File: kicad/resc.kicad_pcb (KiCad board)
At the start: 4 copper layers, 70 x 85 mm, 166 parts, among them J1 CAN, J10 LED2, J2 HALL, J3 COMM, J4 SERVO, J5 SWD, J6 Conn_Coaxial, J7 USB_C_Receptacle_USB2.0_14P, J8 POWER BTN, J9 LED1, Q1 DMN62D0UW-7, Q2 IRF7749L1, Q3 IRF7749L1, Q4 IRF7749L1, Q5 IRF7749L1, Q6 IRF7749L1, Q7 IRF7749L1, SW1 SENSOR_VOLTAGE, U1 DRV8301DCAR, U10 AD8418, U11 SN74LVC1G66DCKR, U12 SN74LVC1G66DCKR, U13 SN74LVC1G66DCKR, U14 TC2117-3.3VDBTR, U15 USBLC6-2SC6, U16 NRF52832-QFAA-R, U2 STM32F405RGTx, U3 TJA1051T-3, U4 SN74LVC1G66DCKR, U5 SN74LVC1G66DCKR, U6 SN74LVC1G66DCKR, U7 BMI160, U8 AD8418, U9 AD8418, Y1 32MHz, Y2 8MHz

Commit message: checking shunt footprints
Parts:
- removed REF1, REF2, REF3, REF4: MountingHole_3.2mm_M3, MountingHole:MountingHole_3.2mm_M3
- added C26: 22nF, Capacitor_SMD:C_0402_1005Metric, F.Cu at (-39.4, 135.4)
- added C33: 15nF, Capacitor_SMD:C_0402_1005Metric, F.Cu at (-33.6, 125.6)
- added C34: 2.2uF, Capacitor_SMD:C_0402_1005Metric, F.Cu at (-33.6, 127.5)
- added C67: 1uF, Capacitor_SMD:C_0402_1005Metric, F.Cu at (-28.0, 162.3)
- added C68: 0.8pF, Capacitor_SMD:C_0402_1005Metric, F.Cu at (-28.0, 164.3)
- added TP6: PH_C, TestPoint:TestPoint_Pad_4.0x4.0mm, F.Cu at (-74.5, 104.7)
- added TP7: GND, TestPoint:TestPoint_Pad_4.0x4.0mm, F.Cu at (-74.5, 110.8)
- C1: value 2.2uF -> 100nF; moved to F.Cu
- C10, C36, C37, C5: value 4.7uF 100V -> 2.2uF; footprint Capacitor_SMD:C_1210_3225Metric -> Capacitor_SMD:C_0402_1005Metric
- C11: value 220nF -> 100nF; moved to F.Cu
- C13: value 2.2uF -> 15pF
- C14: value 15pF -> 2.2uF
- C15: value 100nF -> 2.2uF
- C2, C6, C7, C8, C9, D3, L1, TH1, U10, U11, U12, U13, U8, U9: moved to F.Cu
- C20: value 2.2uF -> 100uF; footprint Capacitor_SMD:C_0402_1005Metric -> Capacitor_SMD:CP_Elec_5x5.4
- C21, C22, C35: value 2.2uF -> 100nF
- C23: value 220nF -> 4.7uF 100V; footprint Capacitor_SMD:C_0402_1005Metric -> Capacitor_SMD:C_1210_3225Metric; moved to F.Cu
- C24: value 220nF -> 1uF; moved to F.Cu
- C25: value 100nF -> 4.7uF 100V; footprint Capacitor_SMD:C_0402_1005Metric -> Capacitor_SMD:C_1210_3225Metric; moved to F.Cu
- C27: value 2.2uF -> 220nF
- C28: value 22nF -> 220nF; moved to F.Cu
- C29: value 15nF -> 220nF; moved to F.Cu
- C3: value 120pF -> 100nF; moved to F.Cu
- C31: value 100nF -> 120pF
- C32: value 100nF -> 6.8nF
- C38, C41: value 2.2uF -> 4.7uF 100V; footprint Capacitor_SMD:C_0402_1005Metric -> Capacitor_SMD:C_1210_3225Metric
- C4: value 6.8nF -> 2.2uF; moved to F.Cu
- C44: value 1nF -> 2.2uF
- C45, C46: value 15nF -> 2.2uF; moved to F.Cu
- C48: value 15nF -> 1nF; moved to F.Cu
- C50: value 2.2uF -> 15nF
- C51, C52: value 470uF 63V -> 15nF; footprint Capacitor_SMD:CP_Elec_16x17.5 -> Capacitor_SMD:C_0402_1005Metric; moved to F.Cu
- C53: value 2.2uF -> 220uF 63V; footprint Capacitor_SMD:C_0402_1005Metric -> footprints:CHEMI-KG5; moved to F.Cu
- C54: value 2.2uF -> 220uF 63V; footprint Capacitor_SMD:C_0402_1005Metric -> footprints:CHEMI-KG5
- C55: value 100uF -> 100uF 63V; footprint Capacitor_SMD:CP_Elec_5x5.4 -> Capacitor_SMD:CP_Elec_8x10.5; moved to F.Cu
- C56: value 100nF -> 100uF 63V; footprint Capacitor_SMD:C_0402_1005Metric -> Capacitor_SMD:CP_Elec_8x10.5
- C57: value 8pF -> 100uF 63V; footprint Capacitor_SMD:C_0402_1005Metric -> Capacitor_SMD:CP_Elec_8x10.5
- C58: value 8pF -> 2.2uF
- C59: value 4.7uF -> 2.2uF
- C60: value 4.7uF -> 100uF; footprint Capacitor_SMD:C_0402_1005Metric -> Capacitor_SMD:CP_Elec_5x5.4
- C61: value 100pF -> 100nF
- C62: value 1uF -> 8pF
- C63: value 0.8pF -> 4.7uF
- C64: value 100nF -> 4.7uF
- C65: value 100nF -> 8pF
- C66: value 2.2uF -> 100pF
- D1: value ~ -> GREEN; footprint Diode_SMD:D_SOD-323 -> LED_SMD:LED_0603_1608Metric; moved to F.Cu
- D2: value TVS 5V -> BLUE; footprint footprints:SOD-123FL -> LED_SMD:LED_0603_1608Metric; moved to F.Cu
- D4: value GREEN -> D_Schottky; footprint LED_SMD:LED_0603_1608Metric -> Diode_SMD:D_SOD-323; moved to F.Cu
- D5: value BLUE -> D_Schottky; footprint LED_SMD:LED_0603_1608Metric -> Diode_SMD:D_SOD-323; moved to F.Cu
- D6: value D_Schottky -> 3.6v
- D7: value 3.6v -> D_Schottky
- D8: value D_Schottky -> ~
- D9: value D_Schottky -> TVS 5V; footprint Diode_SMD:D_SOD-323 -> footprints:SOD-123FL
- J10: value LED2 -> Conn_Coaxial; footprint Connector_JST:JST_PH_B3B-PH-K_1x03_P2.00mm_Vertical -> Connector_Coaxial:U.FL_Molex_MCRF_73412-0110_Vertical
- J4: value SERVO -> POWER BTN; footprint Connector_JST:JST_PH_B3B-PH-K_1x03_P2.00mm_Vertical -> Connector_JST:JST_PH_B2B-PH-K_1x02_P2.00mm_Vertical
- J5: value SWD -> SERVO; footprint Connector_JST:JST_PH_B5B-PH-K_1x05_P2.00mm_Vertical -> Connector_JST:JST_PH_B3B-PH-K_1x03_P2.00mm_Vertical
- J6: value Conn_Coaxial -> SWD; footprint Connector_Coaxial:U.FL_Molex_MCRF_73412-0110_Vertical -> Connector_JST:JST_PH_B5B-PH-K_1x05_P2.00mm_Vertical
- J7: value USB_C_Receptacle_USB2.0_14P -> LED1; footprint Connector_USB:USB_C_Receptacle_G-Switch_GT-USB-7010ASV -> Connector_JST:JST_PH_B3B-PH-K_1x03_P2.00mm_Vertical
- J8: value POWER BTN -> LED2; footprint Connector_JST:JST_PH_B2B-PH-K_1x02_P2.00mm_Vertical -> Connector_JST:JST_PH_B3B-PH-K_1x03_P2.00mm_Vertical
- J9: value LED1 -> USB_C_Receptacle_USB2.0_14P; footprint Connector_JST:JST_PH_B3B-PH-K_1x03_P2.00mm_Vertical -> Connector_USB:USB_C_Receptacle_G-Switch_GT-USB-7010ASV
- Q1: value DMN62D0UW-7 -> IRF7749L1; footprint Package_TO_SOT_SMD:SOT-23 -> Package_DirectFET:DirectFET_L6
- Q2, Q3, Q4, Q5, Q6: footprint Custom:TRANS_BSC014N04LSIATMA1_Custom -> Package_DirectFET:DirectFET_L6; moved to F.Cu
- Q7: value IRF7749L1 -> DMN62D0UW-7; footprint Custom:TRANS_BSC014N04LSIATMA1_Custom -> Package_TO_SOT_SMD:SOT-23; moved to F.Cu
- R1: value 220R -> 10k; moved to F.Cu
- R10: value 39k 60V -> 39k; moved to F.Cu
- R11: value 39k 60V -> 1k; moved to F.Cu
- R12: value 2.2k -> 56k
- R13: value 39k 60V -> 220R; moved to F.Cu
- R14: value 2.2k -> 220R
- R15: value 10k -> 1k PTC; moved to F.Cu
- R16: value 0.0005R -> 1k PTC; footprint footprints:RESC10052X105N -> Resistor_SMD:R_0402_1005Metric; moved to F.Cu
- R17, R18: value 4.7R -> 220R; moved to F.Cu
- R19: value 0.0005R -> 39k 60V; footprint footprints:RESC10052X105N -> Resistor_SMD:R_0402_1005Metric; moved to F.Cu
- R2: value 220k -> 2.2k; moved to F.Cu
- R20: value 4.7R -> 2.2k; moved to F.Cu
- R21: value 4.7R -> 220k; moved to F.Cu
- R22: value 0.0005R -> 18k; footprint footprints:RESC10052X105N -> Resistor_SMD:R_0402_1005Metric; moved to F.Cu
- R23: value 4.7R -> 39k 60V; moved to F.Cu
- R24: value 4.7R -> 3.3k; moved to F.Cu
- R25: value 1k -> 10k; moved to F.Cu
- R26: value 1k -> 2.2k; moved to F.Cu
- R27: value 1k -> 15k; moved to F.Cu
- R29: value 220R -> 39k 60V; moved to F.Cu
- R3: value 15k -> 2.2k; moved to F.Cu
- R30: value 220R -> 2.2k; moved to F.Cu
- R31: value 1k -> 4.7R; moved to F.Cu
- R32, R33: value 2.2k -> 4.7R
- R34: value 2.2k -> 0.0005R; footprint Resistor_SMD:R_0402_1005Metric -> Resistor_SMD:R_Shunt_Isabellenhuette_BVR4026
- R35: value 10k -> 0.0005R; footprint Resistor_SMD:R_0402_1005Metric -> Resistor_SMD:R_Shunt_Isabellenhuette_BVR4026
- R36: value 5.1k -> 0.0005R; footprint Resistor_SMD:R_0402_1005Metric -> Resistor_SMD:R_Shunt_Isabellenhuette_BVR4026
- R37: value 5.1k -> 4.7R
- R38, R39: value 1k -> 4.7R
- R4: value 18k -> 2.2k; moved to F.Cu
- R40: value 39k -> 1k
- R41: value 56k -> 1k
- R42: value 220R -> 1k
- R43: value 1k PTC -> 39k
- R44: value 1k PTC -> 2.2k
- R45, R46: value 220R -> 5.1k
- R5: value 3.3k -> 220R; moved to F.Cu
- R6: value 2.2k -> 1k
- R7: value 39k -> 220R
- R8: value 10k -> 1k; moved to F.Cu
- R9: value 2.2k -> 10k
- TP1: value PH_A -> + SUPPLY; moved to F.Cu
- TP2: value SUPPLY -> - SUPPLY; moved to F.Cu
- TP3: value GND -> SUPPLY; footprint footprints:TestPoint_Pad_7.0x7.0mm -> TestPoint:TestPoint_Pad_4.0x4.0mm
- TP4: value PH_B -> PH_A; footprint footprints:TestPoint_Pad_7.0x7.0mm -> TestPoint:TestPoint_Pad_4.0x4.0mm; moved to F.Cu
- TP5: value PH_C -> PH_B; footprint footprints:TestPoint_Pad_7.0x7.0mm -> TestPoint:TestPoint_Pad_4.0x4.0mm; moved to F.Cu
- U1: value DRV8301DCAR -> STM32F405RGTx; footprint footprints:SOP50P810X120-57N -> Package_QFP:LQFP-64_10x10mm_P0.5mm; moved to F.Cu
- U2: value STM32F405RGTx -> TJA1051T-3; footprint Package_QFP:LQFP-64_10x10mm_P0.5mm -> Package_SO:SOIC-8_3.9x4.9mm_P1.27mm
- U3: value TJA1051T-3 -> SN74LVC1G66DCKR; footprint Package_SO:SOIC-8_3.9x4.9mm_P1.27mm -> footprints:SOT65P210X110-5N; moved to F.Cu
- U4: value SN74LVC1G66DCKR -> DRV8301DCAR; footprint footprints:SOT65P210X110-5N -> footprints:SOP50P810X120-57N
- Y1: value 32MHz -> 8MHz
- Y2: value 8MHz -> 32MHz; footprint Crystal:Crystal_SMD_3225-4Pin_3.2x2.5mm -> Crystal:Crystal_SMD_2016-4Pin_2.0x1.6mm
- moved J5 252.2 mm to (-86.2, 145.9), turned to 0 degrees
- moved D2 250.3 mm to (-87.1, 166.7)
- moved J3 248.3 mm to (-86.2, 139.3), turned to 0 degrees
- moved R1 242.1 mm to (-69.8, 157.3), turned to 0 degrees
- moved J8 241.3 mm to (-86.2, 159.0)
- moved SW1 240.8 mm to (-75.7, 167.5), turned to 0 degrees
- moved J1 234.2 mm to (-66.2, 139.3), turned to 0 degrees
- moved J2 229.6 mm to (-68.2, 145.9), turned to 0 degrees
- moved D3 228.5 mm to (-87.1, 169.3), turned to 0 degrees
- moved R5 223.9 mm to (-69.8, 165.2)
- moved R4 223.7 mm to (-69.8, 163.2), turned to 0 degrees
- moved D1 223.3 mm to (-87.1, 164.1), turned to 0 degrees
- moved C2 223.1 mm to (-56.8, 159.2)
- moved R3 222.6 mm to (-69.8, 161.2)
- moved R2 222.4 mm to (-69.8, 159.3), turned to 0 degrees
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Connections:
- C1 pad 1: +5V -> /MCU/TEMP_MOTOR
- C10 pad 1: SUPPLY -> VDD
- C11 pad 1: /Gate Driver/BST_A -> /MCU/NRST
- C11 pad 2: /SH_A -> GND
- C12 pad 1: Net-(U2-PH0) -> Net-(U1-PH0)
- C13 pad 1: Net-(U2-VCAP_1) -> Net-(U1-PH1)
- C14 pad 1: Net-(U2-PH1) -> Net-(U1-VCAP_1)
- C15 pad 1: /MCU/NRST -> Net-(U1-VCAP_2)
- C16 pad 1: Net-(U2-VCAP_2) -> +5V
- C17 pad 1: VDD -> VCC
- C18 pad 1: VDD -> +5V
- C19 pad 1: VDD -> Net-(U4-DVDD)
- C2 pad 1: VCC -> /TEMP
- C20 pad 1: VDD -> +5V
- C21 pad 1: VDD -> Net-(D8-K)
- C21 pad 2: GND -> Net-(U4-BST_BK)
- C22 pad 1: VDD -> /Gate Driver/SENS_A
- C22 pad 2: GND -> Net-(U3-A)
- C23 pad 1: /Gate Driver/BST_B -> SUPPLY
- C23 pad 2: /Gate Driver/SH_B -> GND
- C24 pad 1: /Gate Driver/BST_C -> Net-(U4-AVDD)
- C24 pad 2: /Gate Driver/SH_C -> GND
- C25 pad 1: Net-(D1-K) -> SUPPLY
- C25 pad 2: Net-(U1-BST_BK) -> GND
- C27 pad 1: +5V -> /Gate Driver/BST_A
- C27 pad 2: GND -> /SH_A
- C28 pad 1: Net-(U1-CP2) -> /Gate Driver/BST_B
- C28 pad 2: Net-(U1-CP1) -> /Gate Driver/SH_B
- C29 pad 1: Net-(U1-SS_TR) -> /Gate Driver/BST_C
- C29 pad 2: GND -> /Gate Driver/SH_C
- C3 pad 1: /Gate Driver/COMP -> /EN_BUCK
- C30 pad 1: /Gate Driver/SENS_A -> /Gate Driver/SENS_B
- C30 pad 2: Net-(U4-A) -> Net-(U5-A)
- C31 pad 1: /Gate Driver/SENS_B -> /Gate Driver/COMP
- C31 pad 2: Net-(U5-A) -> GND
- C32 pad 1: /Gate Driver/SENS_C -> Net-(C32-Pad1)
- C32 pad 2: Net-(U6-A) -> GND
- C35 pad 1: VDD -> /Gate Driver/SENS_C
- C35 pad 2: GND -> Net-(U6-A)
- C36 pad 1: SUPPLY -> VDD
- C37 pad 1: SUPPLY -> VDD
- C38 pad 1: VDD -> SUPPLY
- C4 pad 1: Net-(C4-Pad1) -> Net-(D5-A)
- C41 pad 1: VDD -> SUPPLY
- C44 pad 1: /MCU/CURRENT_1 -> VDD
- C45 pad 1: Net-(U11-B) -> VDD
- C46 pad 1: Net-(U12-B) -> VDD
- C47 pad 1: /MCU/CURRENT_2 -> /MCU/CURRENT_1
- C48 pad 1: Net-(U13-B) -> /MCU/CURRENT_2
- C5 pad 1: SUPPLY -> VDD
- C50 pad 1: /TEMP -> Net-(U11-B)
- C51 pad 1: SUPPLY -> Net-(U12-B)
- C52 pad 1: SUPPLY -> Net-(U13-B)
- C53 pad 1: +5V -> SUPPLY
- C54 pad 1: VDD -> SUPPLY
- C55 pad 1: VDD -> SUPPLY
- C56 pad 1: /MCU/TEMP_MOTOR -> SUPPLY
- C57 pad 1: GND -> SUPPLY
- C57 pad 2: Net-(U16-XC1) -> GND
- C58 pad 1: GND -> +5V
- C58 pad 2: Net-(U16-XC2) -> GND
- C59 pad 1: GND -> VDD
- C59 pad 2: VDD -> GND
- C6 pad 1: Net-(U1-AVDD) -> VDD
- C60 pad 1: GND -> VDD
- C60 pad 2: Net-(U16-DEC1) -> GND
- C61 pad 2: Net-(U16-DEC3) -> VDD
- C62 pad 2: Net-(U16-DEC4) -> Net-(U16-XC1)
- C63 pad 1: Net-(U16-ANT) -> GND
- C63 pad 2: GND -> VDD
- C64 pad 2: VDD -> Net-(U16-DEC1)
- C65 pad 1: /EN_BUCK -> GND
- C65 pad 2: GND -> Net-(U16-XC2)
- C66 pad 1: Net-(D8-A) -> GND
- C66 pad 2: GND -> Net-(U16-DEC3)
- C7 pad 1: Net-(U1-GVDD) -> VDD
- C8 pad 1: Net-(U1-GVDD) -> VDD
- C9 pad 1: Net-(U1-DVDD) -> VDD
- D1 pad 2: GND -> /MCU/LED_GREEN
- D2 pad 1: +5V -> Net-(D2-K)
- D2 pad 2: GND -> VDD
- D4 pad 2: /MCU/LED_GREEN -> /SH_A
- D5 pad 2: VDD -> Net-(D5-A)
- D6 pad 1: Net-(D6-K) -> /EN_BUCK
- D6 pad 2: /SH_A -> GND
- D7 pad 1: /EN_BUCK -> Net-(D5-A)
- D8 pad 2: Net-(D8-A) -> GND
- D9 pad 1: Net-(D8-A) -> +5V
- J10 pad 1: GND -> Net-(J10-In)
- J10 pad 2: Net-(J10-Pin_2) -> GND
- J4 pad 1: GND -> VDD
- J4 pad 2: +5V -> /CONN_SW
- J5 pad 1: /MCU/NRST -> GND
- J5 pad 2: /MCU/SWDIO -> +5V
- J5 pad 3: GND -> /MCU/SERVO
- J6 pad 1: Net-(J6-In) -> /MCU/NRST
- J6 pad 2: GND -> /MCU/SWDIO
- J8 pad 2: /CONN_SW -> Net-(J8-Pin_2)
- L1 pad 2: Net-(D1-K) -> Net-(D8-K)
- L2 pad 2: Net-(J6-In) -> Net-(J10-In)
- Q1 pad 1: +5V -> (no net)
- Q1 pad 2: /MCU/AN_IN -> (no net)
- Q1 pad 3: Net-(Q1-D) -> (no net)
- R1 pad 1: /CAN/CANH -> VDD
- R1 pad 2: /CAN/CANL -> /MCU/TEMP_MOTOR
- R10 pad 1: /Gate Driver/SENS_A -> /EN_BUCK
- R10 pad 2: /SH_A -> Net-(D4-K)
- R11 pad 1: /Gate Driver/SENS_B -> VDD
- R11 pad 2: /Gate Driver/SH_B -> /IMU/SDA
- R12 pad 1: /Gate Driver/SENS_B -> /EN_BUCK
- R12 pad 2: GND -> Net-(D5-K)
- R13 pad 1: /Gate Driver/SENS_C -> Net-(D5-A)
- R13 pad 2: /Gate Driver/SH_C -> /SHUTDOWN
- R14 pad 1: /Gate Driver/SENS_C -> /MCU/LED1
- R14 pad 2: GND -> Net-(J7-Pin_2)
- R15 pad 1: /Gate Driver/EN_GATE -> Net-(D5-K)
- R15 pad 2: GND -> Net-(R15-Pad2)
- R16 pad 1: /SH_A -> /CONN_SW
- R16 pad 2: /Shunt Amplifiers/PH_A -> Net-(R15-Pad2)
- R17 pad 1: /Gate Driver/GH_A -> /MCU/LED2
- R17 pad 2: Net-(Q2-PadG) -> Net-(J8-Pin_2)
- R18 pad 1: /Gate Driver/GL_A -> /CAN/CANH
- R18 pad 2: Net-(Q3-PadG) -> /CAN/CANL
- R19 pad 1: /Gate Driver/SH_B -> /Gate Driver/SENS_A
- R19 pad 2: /Shunt Amplifiers/PH_B -> /SH_A
- R2 pad 1: GND -> /MCU/HALL_1
- R2 pad 2: Net-(U1-RT_CLK) -> Net-(J2-Pin_6)
- R20 pad 1: /Gate Driver/GH_B -> /Gate Driver/SENS_A
- R20 pad 2: Net-(Q4-PadG) -> GND
- R21 pad 1: /Gate Driver/GL_B -> GND
- R21 pad 2: Net-(Q5-PadG) -> Net-(U4-RT_CLK)
- R22 pad 1: /Gate Driver/SH_C -> +5V
- R22 pad 2: /Shunt Amplifiers/PH_C -> Net-(U4-VSENSE)
- R23 pad 1: /Gate Driver/GH_C -> /Gate Driver/SENS_B
- R23 pad 2: Net-(Q6-PadG) -> /Gate Driver/SH_B
- R24 pad 1: /Gate Driver/GL_C -> Net-(U4-VSENSE)
- R24 pad 2: Net-(Q7-PadG) -> GND
- R25 pad 1: /MCU/CURRENT_1 -> Net-(U4-DTC)
- R25 pad 2: /Shunt Amplifiers/C_A -> GND
- R26 pad 1: /MCU/CURRENT_2 -> /Gate Driver/SENS_B
- R26 pad 2: /Shunt Amplifiers/C_B -> GND
- R27 pad 1: /MCU/CURRENT_3 -> /Gate Driver/COMP
- R27 pad 2: /Shunt Amplifiers/C_C -> Net-(C32-Pad1)
- R28 pad 1: /TEMP -> /Gate Driver/EN_GATE
- R29 pad 1: GND -> /Gate Driver/SENS_C
- R29 pad 2: Net-(D3-K) -> /Gate Driver/SH_C
- R3 pad 1: /Gate Driver/COMP -> /MCU/HALL_2
- R3 pad 2: Net-(C4-Pad1) -> Net-(J2-Pin_6)
- R30 pad 1: GND -> /Gate Driver/SENS_C
- R30 pad 2: Net-(D4-K) -> GND
- R31 pad 1: Net-(D5-K) -> /Gate Driver/GH_A
- R31 pad 2: GND -> Net-(Q1-PadG)
- R32 pad 1: /MCU/HALL_1 -> /Gate Driver/GH_B
- R32 pad 2: Net-(J2-Pin_6) -> Net-(Q2-PadG)
- R33 pad 1: /MCU/HALL_2 -> /Gate Driver/GH_C
- R33 pad 2: Net-(J2-Pin_6) -> Net-(Q3-PadG)
- R34 pad 1: /MCU/HALL_3 -> /SH_A
- R34 pad 2: Net-(J2-Pin_6) -> /Shunt Amplifiers/PH_A
- R35 pad 1: VDD -> /Gate Driver/SH_B
- R35 pad 2: /MCU/TEMP_MOTOR -> /Shunt Amplifiers/PH_B
- R36 pad 1: Net-(J7-CC2) -> /Gate Driver/SH_C
- R36 pad 2: GND -> /Shunt Amplifiers/PH_C
- R37 pad 1: Net-(J7-CC1) -> /Gate Driver/GL_A
- R37 pad 2: GND -> Net-(Q4-PadG)
- R38 pad 1: VDD -> /Gate Driver/GL_B
- R38 pad 2: /IMU/SCL -> Net-(Q5-PadG)
- R39 pad 1: VDD -> /Gate Driver/GL_C
- R39 pad 2: /IMU/SDA -> Net-(Q6-PadG)
- R4 pad 1: +5V -> /MCU/HALL_3
- R4 pad 2: Net-(U1-VSENSE) -> Net-(J2-Pin_6)
- R40 pad 1: /EN_BUCK -> /MCU/CURRENT_1
- R40 pad 2: Net-(D6-K) -> /Shunt Amplifiers/C_A
- R41 pad 1: /EN_BUCK -> /MCU/CURRENT_2
- R41 pad 2: Net-(D8-K) -> /Shunt Amplifiers/C_B
- R42 pad 1: Net-(D8-A) -> /MCU/CURRENT_3
- R42 pad 2: /SHUTDOWN -> /Shunt Amplifiers/C_C
- R43 pad 1: Net-(D8-K) -> SUPPLY
- R43 pad 2: Net-(R43-Pad2) -> Net-(Q7-D)
- R44 pad 1: /CONN_SW -> /MCU/AN_IN
- R44 pad 2: Net-(R43-Pad2) -> GND
- R45 pad 1: /MCU/LED1 -> Net-(J9-CC1)
- R45 pad 2: Net-(J9-Pin_2) -> GND
- R46 pad 1: /MCU/LED2 -> Net-(J9-CC2)
- R46 pad 2: Net-(J10-Pin_2) -> GND
- R5 pad 1: Net-(U1-VSENSE) -> GND
- R5 pad 2: GND -> Net-(D1-K)
- R6 pad 1: /MCU/AN_IN -> Net-(D2-K)
- R7 pad 1: SUPPLY -> GND
- R7 pad 2: Net-(Q1-D) -> Net-(D3-K)
- R8 pad 1: Net-(U1-DTC) -> VDD
- R8 pad 2: GND -> /IMU/SCL
- R9 pad 1: /Gate Driver/SENS_A -> /TEMP
- TP1 pad 1: /Shunt Amplifiers/PH_A -> /SUPPLY
- TP2 pad 1: SUPPLY -> GND
- TP3 pad 1: GND -> SUPPLY
- TP4 pad 1: /Shunt Amplifiers/PH_B -> /Shunt Amplifiers/PH_A
- TP5 pad 1: /Shunt Amplifiers/PH_C -> /Shunt Amplifiers/PH_B
- U1 pad 1: Net-(U1-RT_CLK) -> VDD
- U1 pad 10: /Gate Driver/SDO -> /MCU/CURRENT_3
- U1 pad 11: /Gate Driver/SCLK -> /MCU/AN_IN
- U1 pad 12: unconnected-(U1-DC_CAL-Pad12) -> GND
- U1 pad 13: Net-(U1-GVDD) -> VDD
- U1 pad 14: Net-(U1-CP1) -> /Gate Driver/SENS_A
- U1 pad 15: Net-(U1-CP2) -> /Gate Driver/SENS_B
- U1 pad 16: /Gate Driver/EN_GATE -> /Gate Driver/SENS_C
- U1 pad 17: /Gate Driver/INH_A -> /TEMP
- U1 pad 18: /Gate Driver/INL_A -> GND
- U1 pad 19: /Gate Driver/INH_B -> VDD
- U1 pad 2: /Gate Driver/COMP -> /Gate Driver/SENS_FILTERED
- U1 pad 20: /Gate Driver/INL_B -> /BLE/SWDCLK
- U1 pad 21: /Gate Driver/INH_C -> /MCU/SCK_ADC_EXT
- U1 pad 22: /Gate Driver/INL_C -> /MCU/MISO_ADC_EXT2
- U1 pad 23: Net-(U1-DVDD) -> /MCU/TX_SCL_MOSI
- U1 pad 24: Net-(U1-AVDD) -> /MCU/TEMP_MOTOR
- U1 pad 25: unconnected-(U1-SO1-Pad25) -> /SHUTDOWN
- U1 pad 26: unconnected-(U1-SO2-Pad26) -> /MCU/LED_GREEN
- U1 pad 27: Net-(U1-AVDD) -> /MCU/LED_RED
- U1 pad 28: GND -> /IMU/SDA
- U1 pad 29: SUPPLY -> /MCU/TX_SCL_MOSI
- U1 pad 3: Net-(U1-VSENSE) -> /MCU/LED1
- U1 pad 30: GND -> /MCU/RX_SDA_NSS
- U1 pad 31: GND -> Net-(U1-VCAP_1)
- U1 pad 32: GND -> VDD
- U1 pad 33: GND -> /BLE/SWDIO
- U1 pad 34: GND -> /Gate Driver/INL_A
- U1 pad 35: /Gate Driver/GL_C -> /Gate Driver/INL_B
- U1 pad 36: /Gate Driver/SH_C -> /Gate Driver/INL_C
- U1 pad 37: /Gate Driver/GH_C -> /MCU/HALL_1
- U1 pad 38: /Gate Driver/BST_C -> /MCU/HALL_2
- U1 pad 39: GND -> /MCU/HALL_3
- U1 pad 4: unconnected-(U1-PWRGD-Pad4) -> /MCU/LED2
- U1 pad 40: /Gate Driver/GL_B -> /Gate Driver/CS
- U1 pad 41: /Gate Driver/SH_B -> /Gate Driver/INH_A
- U1 pad 42: /Gate Driver/GH_B -> /Gate Driver/INH_B
- U1 pad 43: /Gate Driver/BST_B -> /Gate Driver/INH_C
- U1 pad 44: GND -> /MCU/USB_DM
- U1 pad 45: /Gate Driver/GL_A -> /MCU/USB_DP
- U1 pad 46: /SH_A -> /MCU/SWDIO
- U1 pad 47: /Gate Driver/GH_A -> Net-(U1-VCAP_2)
- U1 pad 48: /Gate Driver/BST_A -> VDD
- U1 pad 49: VDD -> /MCU/SWCLK
- U1 pad 5: unconnected-(U1-~{OCTW}-Pad5) -> Net-(U1-PH0)
- U1 pad 50: Net-(D1-K) -> /IMU/SCL
- U1 pad 51: Net-(D1-K) -> /BLE/BLE_RX
- U1 pad 52: Net-(U1-BST_BK) -> /BLE/BLE_TX
- U1 pad 53: SUPPLY -> /Gate Driver/SCLK
- U1 pad 54: SUPPLY -> /MCU/CURR_FILT_ON
- U1 pad 55: /EN_BUCK -> /Gate Driver/SDO
- U1 pad 56: Net-(U1-SS_TR) -> /Gate Driver/SDI
- U1 pad 57: GND -> /Gate Driver/EN_GATE
- U1 pad 6: /Gate Driver/FAULT -> Net-(U1-PH1)
- U1 pad 7: Net-(U1-DTC) -> /MCU/NRST
- U1 pad 8: /Gate Driver/CS -> /MCU/CURRENT_1
- U1 pad 9: /Gate Driver/SDI -> /MCU/CURRENT_2
- U15 pad 4: Net-(J7-D+-PadA6) -> Net-(J9-D+-PadA6)
- U15 pad 6: Net-(J7-D--PadA7) -> Net-(J9-D--PadA7)
- U16 pad 2: /BLE/BLE_TX -> unconnected-(U16-P0_00/XL1-Pad2)
- U16 pad 3: /BLE/BLE_RX -> /BLE/BLE_TX
- U16 pad 4: unconnected-(U16-P0_02/AIN0-Pad4) -> /BLE/BLE_RX
- U2 pad 1: VDD -> /CAN/TX
- U2 pad 2: /Gate Driver/SENS_FILTERED -> GND
- U2 pad 3: /MCU/LED1 -> +5V
- U2 pad 4: /MCU/LED2 -> /CAN/RX
- U2 pad 5: Net-(U2-PH0) -> VCC
- U2 pad 6: Net-(U2-PH1) -> /CAN/CANL
- U2 pad 7: /MCU/NRST -> /CAN/CANH
- U2 pad 8: /MCU/CURRENT_1 -> GND
- U3 pad 1: /CAN/TX -> Net-(U3-A)
- U3 pad 3: +5V -> GND
- U3 pad 4: /CAN/RX -> /Gate Driver/SENS_FILTERED
- U3 pad 5: VCC -> VDD
- U4 pad 1: Net-(U4-A) -> Net-(U4-RT_CLK)
- U4 pad 2: GND -> /Gate Driver/COMP
- U4 pad 3: GND -> Net-(U4-VSENSE)
- U4 pad 4: /Gate Driver/SENS_FILTERED -> unconnected-(U4-PWRGD-Pad4)
- U4 pad 5: VDD -> unconnected-(U4-~{OCTW}-Pad5)
- Y1 pad 1: Net-(U16-XC2) -> Net-(U1-PH0)
- Y1 pad 2: GND -> Net-(U1-PH1)
- Y1 pad 3: Net-(U16-XC1) -> GND
- Y1 pad 4: GND -> (no net)
- Y2 pad 1: Net-(U2-PH0) -> Net-(U16-XC2)
- Y2 pad 2: Net-(U2-PH1) -> GND
- Y2 pad 3: GND -> Net-(U16-XC1)
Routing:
- net VDD: track 313.3 -> 0.00 mm, vias 21 -> 0
- net +5V: track 187.5 -> 0.00 mm, vias 9 -> 0
- net /CONN_SW: track 77.8 -> 0.00 mm, vias 1 -> 0
- net /MCU/CURR_FILT_ON: track 76.4 -> 0.00 mm, vias 5 -> 0
- net /SH_A: track 63.8 -> 0.00 mm, vias 25 -> 0
- net /MCU/CURRENT_3: track 60.7 -> 0.00 mm, vias 3 -> 0
- net /Gate Driver/SENS_C: track 56.9 -> 0.00 mm, vias 5 -> 0
- net /Gate Driver/SENS_B: track 56.3 -> 0.00 mm, vias 4 -> 0
- net /MCU/CURRENT_2: track 55.6 -> 0.00 mm, vias 5 -> 0
- net /MCU/USB_DM: track 54.4 -> 0.00 mm, vias 2 -> 0
- net /MCU/USB_DP: track 54.0 -> 0.00 mm, vias 2 -> 0
- net /Gate Driver/SENS_A: track 50.5 -> 0.00 mm, vias 3 -> 0
- net /Gate Driver/SH_C: track 47.6 -> 0.00 mm, vias 24 -> 0
- net SUPPLY: track 47.0 -> 0.00 mm, vias 156 -> 0
- net /BLE/SWDIO: track 45.5 -> 0.00 mm, vias 2 -> 0
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- removed copper zone on B.Cu, net /Gate Driver/SH_B
- removed copper zone on F.Cu, net /Gate Driver/SH_B
- removed copper zone on In1.Cu, net /Gate Driver/SH_B
- removed copper zone on In2.Cu, net /Gate Driver/SH_B
- removed copper zone on B.Cu, net /Gate Driver/SH_C
- removed copper zone on F.Cu, net /Gate Driver/SH_C
- removed copper zone on In1.Cu, net /Gate Driver/SH_C
- removed copper zone on In2.Cu, net /Gate Driver/SH_C
- removed copper zone on B.Cu, net /SH_A
- removed copper zone on F.Cu, net /SH_A
- removed copper zone on In1.Cu, net /SH_A
- removed copper zone on In2.Cu, net /SH_A
- removed copper zone on B.Cu, net SUPPLY
- removed copper zone on F.Cu, net SUPPLY
- removed copper zone on In1.Cu, net SUPPLY
- removed copper zone on In2.Cu, net SUPPLY
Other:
- board size 70 x 85 mm -> 51.5 x 80 mm
- board text removed: "electronic speed controller by reykato rev 0"
- board text removed: "rESC"

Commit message: forgot to close kicad
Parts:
- removed R34, R35, R36: 0.0005R, Resistor_SMD:R_Shunt_Isabellenhuette_BVR4026

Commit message: working on fet fp
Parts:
- added R34: 0.0005R, footprints:RESC10052X105N, F.Cu at (-65.4, 87.0)
- added R35: 0.0005R, footprints:RESC10052X105N, F.Cu at (-65.4, 94.0)
- added R36: 0.0005R, footprints:RESC10052X105N, F.Cu at (-65.4, 101.1)
- Q1, Q2, Q3, Q4, Q5, Q6: footprint Package_DirectFET:DirectFET_L6 -> footprints:TRANS_BSC014N04LSIATMA1
- TP7: moved to B.Cu
- Y1: footprint Crystal:Crystal_SMD_2016-4Pin_2.0x1.6mm -> Crystal:Crystal_SMD_3225-4Pin_3.2x2.5mm
- moved TP7 196.7 mm to (115.1, 58.5)
- moved TP3 191.7 mm to (115.1, 58.5)
- moved D1 13.8 mm to (-100.9, 164.7)
- moved D2 13.8 mm to (-100.9, 167.3)
- moved D3 13.8 mm to (-100.9, 169.9)
- moved Q6 13.0 mm to (-94.2, 123.2)
- moved Q5 12.1 mm to (-94.2, 116.5)
- moved Q4 11.4 mm to (-94.2, 109.8)
- moved Q1 11.1 mm to (-94.2, 89.7)
- moved Q3 11.0 mm to (-94.2, 103.1)
- moved Q2 10.9 mm to (-94.2, 96.4)
- moved SW1 5.66 mm to (-80.0, 171.2)
- moved Y1 0.38 mm to (-35.2, 163.6)
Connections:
- Q1 pad 1: (no net) -> /SH_A
- Q2 pad 1: (no net) -> /Gate Driver/SH_B
- Q3 pad 1: (no net) -> /Gate Driver/SH_C
- Q4 pad 1: (no net) -> GND
- Q5 pad 1: (no net) -> GND
- Q6 pad 1: (no net) -> GND
- R31 pad 2: Net-(Q1-PadG) -> Net-(Q1-G)
- R32 pad 2: Net-(Q2-PadG) -> Net-(Q2-G)
- R33 pad 2: Net-(Q3-PadG) -> Net-(Q3-G)
- R37 pad 2: Net-(Q4-PadG) -> Net-(Q4-G)
- R38 pad 2: Net-(Q5-PadG) -> Net-(Q5-G)
- R39 pad 2: Net-(Q6-PadG) -> Net-(Q6-G)

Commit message: routing gate driver
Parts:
- removed TP1: + SUPPLY, footprints:TestPoint_Pad_7.0x7.0mm
- removed TP2: - SUPPLY, footprints:TestPoint_Pad_7.0x7.0mm
- added C69: 0.8pF, Capacitor_SMD:C_0402_1005Metric, F.Cu at (-46.5, 113.8)
- added H1: MountingHole, MountingHole:MountingHole_3.2mm_M3, F.Cu at (-29.7, 47.9)
- added H2: MountingHole, MountingHole:MountingHole_3.2mm_M3, F.Cu at (-29.7, 55.8)
- added H3: MountingHole, MountingHole:MountingHole_3.2mm_M3, F.Cu at (-29.7, 63.8)
- added H4: MountingHole, MountingHole:MountingHole_3.2mm_M3, F.Cu at (-29.7, 71.7)
- C21, C27, C28, C29, C33, C47, C48, C49, D8, L1, R34, R35, R36, R40, R41, R42, U10, U8, U9: moved to B.Cu
- C53, C54: value 220uF 63V -> 470uF 63V; footprint footprints:CHEMI-KG5 -> Capacitor_SMD:CP_Elec_16x17.5; moved to B.Cu
- C55, C56: value 100uF 63V -> 2.2uF; footprint Capacitor_SMD:CP_Elec_8x10.5 -> Capacitor_SMD:C_0402_1005Metric
- C57: value 100uF 63V -> 100uF; footprint Capacitor_SMD:CP_Elec_8x10.5 -> Capacitor_SMD:CP_Elec_5x5.4
- C58: value 2.2uF -> 100nF
- C59: value 2.2uF -> 8pF
- C60: value 100uF -> 4.7uF; footprint Capacitor_SMD:CP_Elec_5x5.4 -> Capacitor_SMD:C_0402_1005Metric
- C61: value 100nF -> 4.7uF
- C63: value 4.7uF -> 100pF
- C64: value 4.7uF -> 1uF
- C65: value 8pF -> 0.8pF
- C66: value 100pF -> 8pF
- C67: value 1uF -> 100pF
- C68: value 0.8pF -> 1uF
- Q1, Q2, Q3, Q4, Q5, Q6: footprint footprints:TRANS_BSC014N04LSIATMA1 -> footprints:TRANS_BSC014N04LSIATMA1_Custom
- TP3: footprint TestPoint:TestPoint_Pad_4.0x4.0mm -> footprints:TestPoint_Pad_5.5x4.0mm
- TP4, TP5, TP6: footprint TestPoint:TestPoint_Pad_4.0x4.0mm -> footprints:TestPoint_Pad_5.5x4.0mm; moved to B.Cu
- TP7: footprint TestPoint:TestPoint_Pad_4.0x4.0mm -> footprints:TestPoint_Pad_5.5x4.0mm; moved to F.Cu
- moved J7 270.1 mm to (163.0, 48.3), turned to 180 degrees
- moved J4 268.6 mm to (167.7, 49.4), turned to 90 degrees
- moved J5 268.1 mm to (167.7, 59.9), turned to 90 degrees
- moved J8 264.6 mm to (154.1, 48.3), turned to 180 degrees
- moved J3 258.3 mm to (167.7, 91.7), turned to 90 degrees
- moved R12 253.9 mm to (178.1, 98.4)
- moved R10 253.2 mm to (178.1, 97.2)
- moved J6 249.0 mm to (167.7, 72.8), turned to 90 degrees
- moved D6 248.6 mm to (178.1, 93.1)
- moved C3 243.7 mm to (178.1, 96.0)
- moved Q1 242.9 mm to (148.6, 97.7), turned to 90 degrees
- moved Q4 241.1 mm to (146.8, 104.2)
- moved J2 237.6 mm to (167.7, 117.5), turned to 90 degrees
- moved J1 236.8 mm to (167.7, 102.6), turned to 90 degrees
- moved Q5 231.5 mm to (136.9, 104.2), turned to 180 degrees
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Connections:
- C55 pad 1: SUPPLY -> +5V
- C56 pad 1: SUPPLY -> VDD
- C57 pad 1: SUPPLY -> VDD
- C58 pad 1: +5V -> GND
- C58 pad 2: GND -> VDD
- C59 pad 1: VDD -> GND
- C59 pad 2: GND -> Net-(U16-XC1)
- C60 pad 1: VDD -> GND
- C60 pad 2: GND -> VDD
- C61 pad 2: VDD -> Net-(U16-DEC1)
- C62 pad 2: Net-(U16-XC1) -> Net-(U16-XC2)
- C63 pad 2: VDD -> Net-(U16-DEC3)
- C64 pad 2: Net-(U16-DEC1) -> Net-(U16-DEC4)
- C65 pad 1: GND -> Net-(U16-ANT)
- C65 pad 2: Net-(U16-XC2) -> GND
- C66 pad 2: Net-(U16-DEC3) -> Net-(U16-XC2)
- C67 pad 2: Net-(U16-DEC4) -> Net-(U16-DEC3)
- C68 pad 1: Net-(U16-ANT) -> GND
- C68 pad 2: GND -> Net-(U16-DEC4)
- J4 pad 1: VDD -> GND
- R31 pad 2: Net-(Q1-G) -> Net-(Q1-PadG)
- R32 pad 2: Net-(Q2-G) -> Net-(Q2-PadG)
- R33 pad 2: Net-(Q3-G) -> Net-(Q3-PadG)
- R37 pad 2: Net-(Q4-G) -> Net-(Q4-PadG)
- R38 pad 2: Net-(Q5-G) -> Net-(Q5-PadG)
- R39 pad 2: Net-(Q6-G) -> Net-(Q6-PadG)
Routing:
- net /Gate Driver/SH_C: track 0.00 -> 89.6 mm, vias 0 -> 50
- net +5V: track 0.00 -> 74.3 mm
- net /Gate Driver/SH_B: track 0.00 -> 60.9 mm, vias 0 -> 50
- net /Shunt Amplifiers/PH_C: track 0.00 -> 40.0 mm, vias 0 -> 68
- net Net-(Q3-PadG): track 0.00 -> 39.0 mm
- net Net-(Q6-PadG): track 0.00 -> 36.6 mm
- net /Gate Driver/GL_C: track 0.00 -> 30.7 mm
- net /Shunt Amplifiers/PH_B: track 0.00 -> 26.2 mm, vias 0 -> 68
- net /SH_A: track 0.00 -> 26.1 mm, vias 0 -> 52
- net Net-(Q2-PadG): track 0.00 -> 24.9 mm
- net Net-(Q5-PadG): track 0.00 -> 23.0 mm
- net /Gate Driver/GH_C: track 0.00 -> 22.8 mm
- net /Shunt Amplifiers/PH_A: track 0.00 -> 19.4 mm, vias 0 -> 68
- net /Gate Driver/GH_B: track 0.00 -> 18.3 mm
- net /Gate Driver/GL_B: track 0.00 -> 14.8 mm
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- added copper zone on B.Cu, net /Gate Driver/SH_B
- added copper zone on F.Cu, net /Gate Driver/SH_B
- added copper zone on In1.Cu, net /Gate Driver/SH_B
- added copper zone on In2.Cu, net /Gate Driver/SH_B
- added copper zone on B.Cu, net /Gate Driver/SH_C
- added copper zone on F.Cu, net /Gate Driver/SH_C
- added copper zone on In1.Cu, net /Gate Driver/SH_C
- added copper zone on In2.Cu, net /Gate Driver/SH_C
- added copper zone on B.Cu, net /SH_A
- added copper zone on F.Cu, net /SH_A
- added copper zone on In1.Cu, net /SH_A
- added copper zone on In2.Cu, net /SH_A
- added copper zone on B.Cu, net /Shunt Amplifiers/PH_A
- added copper zone on F.Cu, net /Shunt Amplifiers/PH_A
- added copper zone on In1.Cu, net /Shunt Amplifiers/PH_A
- added copper zone on In2.Cu, net /Shunt Amplifiers/PH_A
- added copper zone on B.Cu, net /Shunt Amplifiers/PH_B
- added copper zone on F.Cu, net /Shunt Amplifiers/PH_B
- added copper zone on In1.Cu, net /Shunt Amplifiers/PH_B
- added copper zone on In2.Cu, net /Shunt Amplifiers/PH_B
- added copper zone on B.Cu, net /Shunt Amplifiers/PH_C
- added copper zone on F.Cu, net /Shunt Amplifiers/PH_C
- added copper zone on In1.Cu, net /Shunt Amplifiers/PH_C
- added copper zone on In2.Cu, net /Shunt Amplifiers/PH_C
- added copper zone on B.Cu, net SUPPLY
- added copper zone on In2.Cu, net SUPPLY
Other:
- board size 51.5 x 80 mm -> 51 x 75 mm

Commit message: gate driver routed to mosfets, working on misc stm32 related components
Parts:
- C17, C20, C36, C37, C38, C40, C57, C59, C61, C62, C64, SW1, TP3, Y2: moved to B.Cu
- C53, C54: footprint Capacitor_SMD:CP_Elec_16x17.5 -> footprints:CP_Elec_16x17.5_Panasonic
- L1: footprint Inductor_SMD:L_0402_1005Metric -> footprints:IND_VLS3010CX-220M-1
- U14: footprint footprints:SOT-223_3MC_MCH -> footprints:SOT-223_3MC_MCH_Custom
- moved SW1 268.2 mm to (164.7, 61.4), turned to -90 degrees
- moved D3 265.1 mm to (146.7, 75.1), turned to 90 degrees
- moved D1 260.6 mm to (143.8, 75.1), turned to 90 degrees
- moved D2 258.8 mm to (141.0, 75.2), turned to 90 degrees
- moved R7 237.2 mm to (148.2, 75.4), turned to -90 degrees
- moved R5 233.0 mm to (145.2, 75.4), turned to -90 degrees
- moved C24 232.2 mm to (187.6, 84.5)
- moved R6 231.2 mm to (142.4, 75.4), turned to 90 degrees
- moved Y1 218.4 mm to (153.2, 53.1), turned to 180 degrees
- moved C20 213.7 mm to (157.8, 83.2), turned to 90 degrees
- moved C12 211.0 mm to (154.6, 55.7)
- moved C13 209.7 mm to (152.1, 55.7), turned to 180 degrees
- moved C42 206.4 mm to (149.4, 88.8), turned to 90 degrees
- moved C65 204.8 mm to (144.2, 47.6), turned to 135 degrees
- moved U14 203.4 mm to (160.4, 54.7), turned to 90 degrees
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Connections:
- C17 pad 1: VCC -> +5V
- U15 pad 5: VBUS -> +5V
- U2 pad 5: VCC -> +5V
- Y1 pad 2: Net-(U1-PH1) -> GND
- Y1 pad 3: GND -> Net-(U1-PH1)
- Y1 pad 4: (no net) -> GND
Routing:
- net +5V: track 74.3 -> 140.4 mm, vias 0 -> 6
- net VDD: track 0.00 -> 47.9 mm, vias 0 -> 6
- net /CAN/CANH: track 0.00 -> 17.8 mm, vias 0 -> 1
- net /CAN/CANL: track 0.00 -> 16.5 mm, vias 0 -> 1
- net SUPPLY: track 6.78 -> 21.2 mm, vias 157 -> 204
- net Net-(D8-K): track 8.38 -> 21.0 mm, vias 1 -> 2
- net Net-(U4-BST_BK): track 0.00 -> 11.5 mm, vias 0 -> 1
- net Net-(U1-PH0): track 0.00 -> 11.4 mm
- net Net-(U1-PH1): track 0.00 -> 9.93 mm
- net Net-(J9-CC1): track 0.00 -> 9.69 mm
- net Net-(U16-XC2): track 0.00 -> 9.48 mm, vias 0 -> 1
- net /MCU/LED_GREEN: track 0.00 -> 7.87 mm
- net Net-(J9-D--PadA7): track 0.00 -> 6.94 mm
- net Net-(J9-CC2): track 0.00 -> 6.79 mm
- net Net-(U16-XC1): track 0.00 -> 6.42 mm, vias 0 -> 1
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
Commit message: done? without test points
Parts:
- removed C66: 8pF, Capacitor_SMD:C_0402_1005Metric
- removed C67: 100pF, Capacitor_SMD:C_0402_1005Metric
- removed C68: 1uF, Capacitor_SMD:C_0402_1005Metric
- removed C69: 0.8pF, Capacitor_SMD:C_0402_1005Metric
- C1, C10, C11, C14, C15, C2, C22, C23, C25, C30, C31, C32, C35, C44, C45, C46, C5, C50, C51, C52, C58, C6, C60, C7, C8, C9, R1, R14, R17, R18, R19, R20, R21, R23, R25, R26, R27, R28, R29, R30, R9: moved to B.Cu
- C59, C62, Y2: moved to F.Cu
- Q1, Q2, Q3, Q4, Q5, Q6: footprint footprints:TRANS_BSC014N04LSIATMA1_Custom -> footprints:TRANS_BSC014N04LSIATMA1_Custom_NoSilkscreen
- U11, U12, U13, U3, U5, U6: footprint footprints:SOT65P210X110-5N -> footprints:SOT65P210X110-5N_Custom; moved to B.Cu
- moved R14 252.6 mm to (156.8, 51.7)
- moved R4 250.3 mm to (163.3, 71.9), turned to 180 degrees
- moved R3 250.0 mm to (163.3, 70.8), turned to 180 degrees
- moved R2 249.7 mm to (163.3, 69.7), turned to 180 degrees
- moved R1 241.8 mm to (155.1, 68.4), turned to -90 degrees
- moved R17 239.1 mm to (148.6, 51.7)
- moved R13 237.9 mm to (164.0, 109.8), turned to 180 degrees
- moved R9 235.1 mm to (148.5, 64.9), turned to -90 degrees
- moved C1 230.3 mm to (156.9, 71.3), turned to 90 degrees
- moved D7 229.3 mm to (163.7, 117.4), turned to 180 degrees
- moved R16 229.0 mm to (160.8, 115.1), turned to 180 degrees
- moved D5 228.9 mm to (163.7, 113.5)
- moved R15 228.8 mm to (160.8, 113.9), turned to 180 degrees
- moved D4 228.7 mm to (163.7, 111.5)
- moved C4 227.4 mm to (164.0, 108.7), turned to 180 degrees
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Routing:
- net VDD: track 47.9 -> 259.7 mm, vias 6 -> 24
- net /MCU/CURRENT_1: track 1.20 -> 90.8 mm, vias 0 -> 4
- net /MCU/CURRENT_3: track 1.32 -> 76.7 mm, vias 0 -> 5
- net /MCU/CURRENT_2: track 2.42 -> 74.6 mm, vias 0 -> 4
- net /CONN_SW: track 0.00 -> 71.9 mm, vias 0 -> 2
- net /MCU/NRST: track 0.00 -> 70.1 mm, vias 0 -> 3
- net /SH_A: track 26.1 -> 93.8 mm, vias 52 -> 58
- net /MCU/SWDIO: track 0.00 -> 57.8 mm, vias 0 -> 3
- net /TEMP: track 0.00 -> 53.4 mm, vias 0 -> 3
- net /SHUTDOWN: track 0.00 -> 52.7 mm, vias 0 -> 2
- net /MCU/SWCLK: track 0.00 -> 45.5 mm, vias 0 -> 1
- net /Gate Driver/FAULT: track 0.00 -> 40.9 mm, vias 0 -> 2
- net /Gate Driver/SDO: track 0.00 -> 40.6 mm, vias 0 -> 4
- net /Gate Driver/SDI: track 0.00 -> 40.3 mm, vias 0 -> 4
- net +5V: track 140.4 -> 180.7 mm, vias 6 -> 8
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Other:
- outline, holes or cut-outs redrawn
- board text added: "2025-08-11"
- board text added: "electronic speed controller by reykato"
- board text added: "rESC"
- board text added: "rev 1"

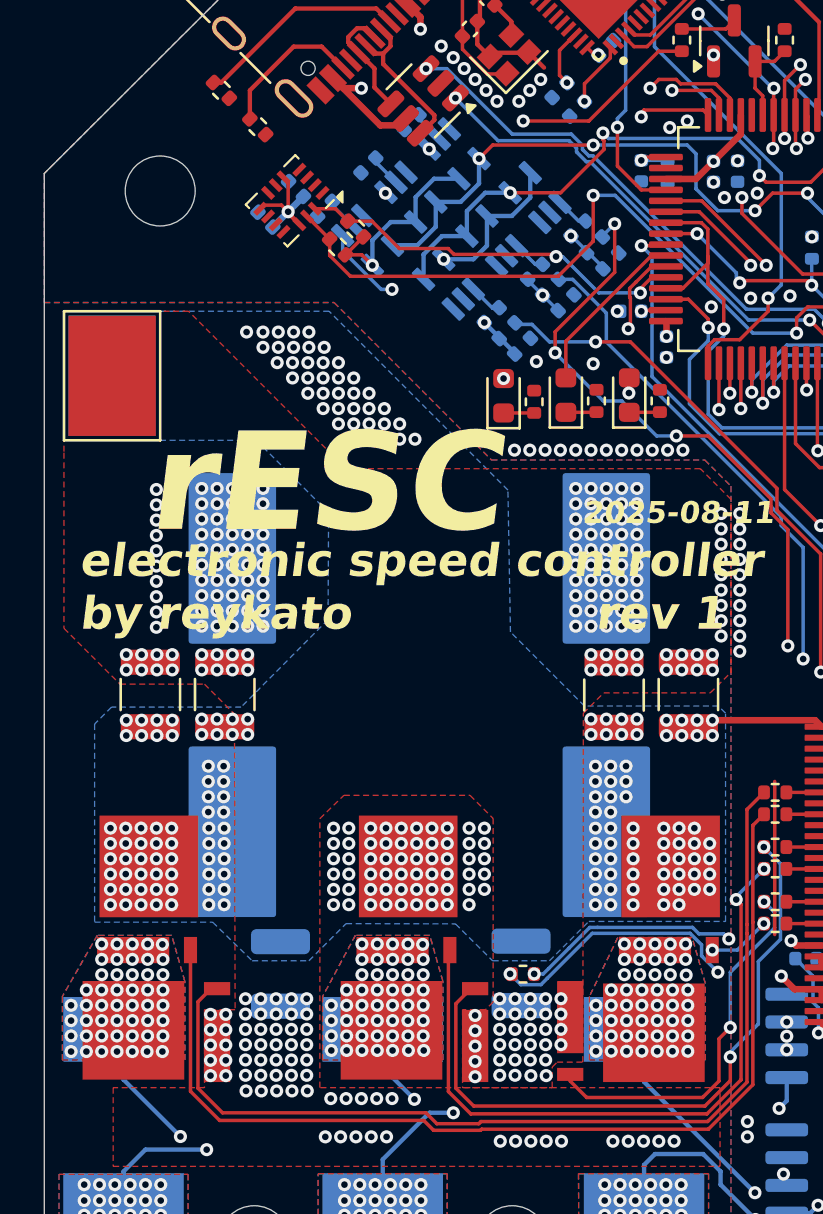
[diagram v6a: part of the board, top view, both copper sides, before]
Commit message: revision 1, drv won't power on right?
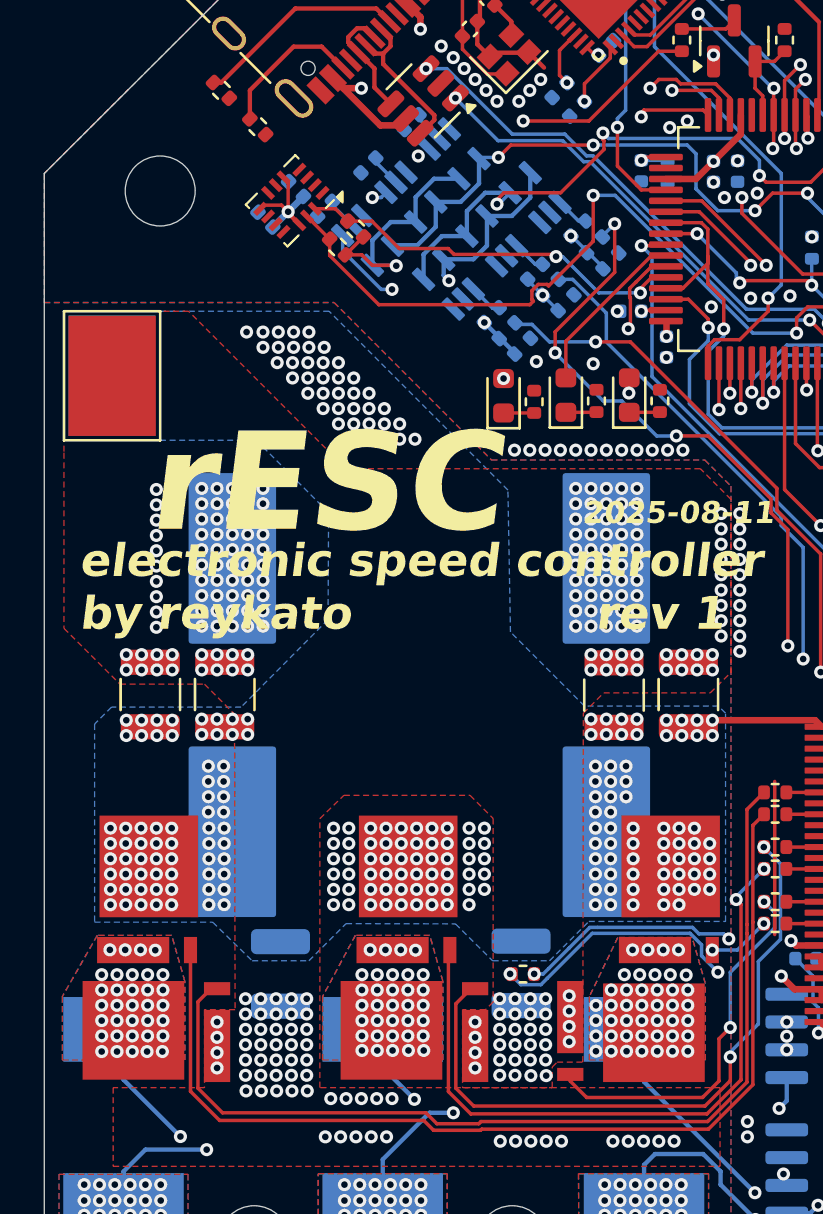
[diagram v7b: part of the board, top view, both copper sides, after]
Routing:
- net VDD: track 259.7 -> 263.9 mm
- net /Gate Driver/SENS_FILTERED: track 27.7 -> 29.4 mm
- net /IMU/SCL: track 35.7 -> 37.2 mm
- net /MCU/CURRENT_2: track 74.6 -> 76.0 mm
- net /MCU/CURRENT_3: track 76.7 -> 77.4 mm
- net GND: vias 397 -> 390
- net /SH_A: vias 58 -> 52
- net /Gate Driver/SH_C: vias 54 -> 39
- net /Gate Driver/SH_B: vias 54 -> 39
